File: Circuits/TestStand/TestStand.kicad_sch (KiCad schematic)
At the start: 2 parts, among them U1 INA125UA

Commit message: HX711 Load Cell Circuitry
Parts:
- removed U1: INA125UA, D16, symbol 2024-08-07_02-08-08:INA125UA
- added C1, C2, C4: 0.1uF, symbol Device:C
- added C3: 10uF, symbol Device:C
- added J1: Screw_Terminal_01x07, symbol Connector:Screw_Terminal_01x07
- added JP1: SolderJumper_2_Bridged, symbol Jumper:SolderJumper_2_Bridged
- added L1: 3.3uH, symbol Device:L
- added Q1: MMBT4403-7-F, SOT96P240X110-3N, symbol MMBT4403-7-F:MMBT4403-7-F
- added R2, R3: 100, symbol Device:R_US
- added R4, R5: 8.2K, symbol Device:R_US
- added U1: HX711, Package_SO:SOP-16_3.9x9.9mm_P1.27mm, symbol Analog_ADC:HX711
- R1: value 10 -> 10K
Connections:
- net at R1.1: now also JP1.2 (B), U1.15 (RATE)
- net +5V: now reaches R1.2
- net +5V: now also Q1.2, U1.1 (VSUP), U1.16 (DVDD)
- new net: C1.1, R3.2, U1.7 (INA-)
- new net: C1.2, R2.2, U1.8 (INA+)
- new net: L1.2, U1.3 (AVDD)
- new net: Q1.1, U1.2 (BASE)
- new net: Q1.3, R5.1
- new net: R4.2, R5.2, U1.4 (VFB)
- new net: C2.1, U1.6 (VBG)
- new net A+: J1.4 (Pin_4), R2.1
- new net A-: J1.5 (Pin_5), R3.1
- new net B+: J1.1 (Pin_1), U1.10 (INB+)
- new net B-: J1.2 (Pin_2), U1.9 (INB-)
- new net DAT: U1.12 (DOUT)
- new net E+: C3.1, C4.1, J1.7 (Pin_7), L1.1
- new net GND: C2.2, C3.2, C4.2, J1.3 (Pin_3), J1.6 (Pin_6), JP1.1 (A), R4.1, U1.14 (XI), U1.5 (AGND)
- new net SCK: U1.11 (PD_SCK)
- no-connect marks 0 -> 1
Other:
- note added: "Closed: 10SPS Open: 80SPS"
- note added: "Load Cell 0 IO and Amplifier"

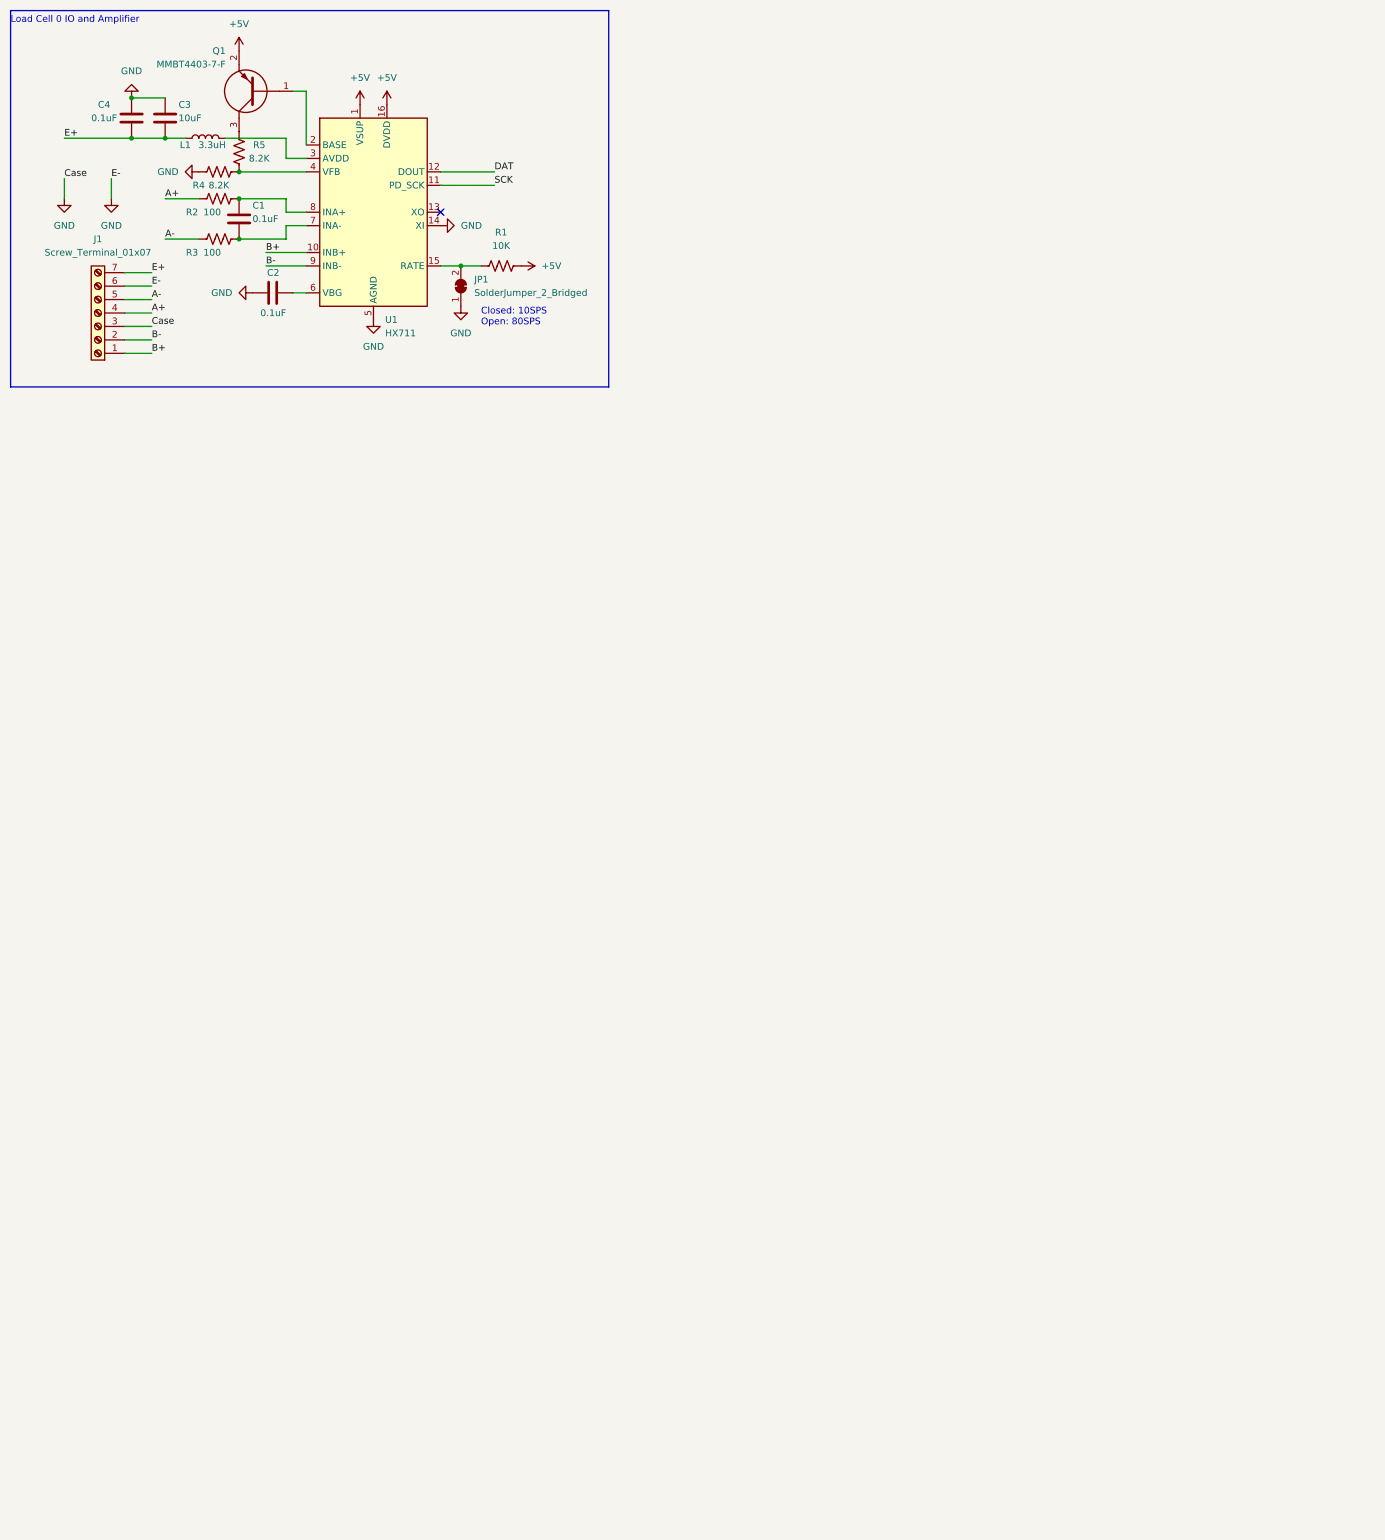
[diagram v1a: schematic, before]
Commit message: Added all 3 load cell amplifiers
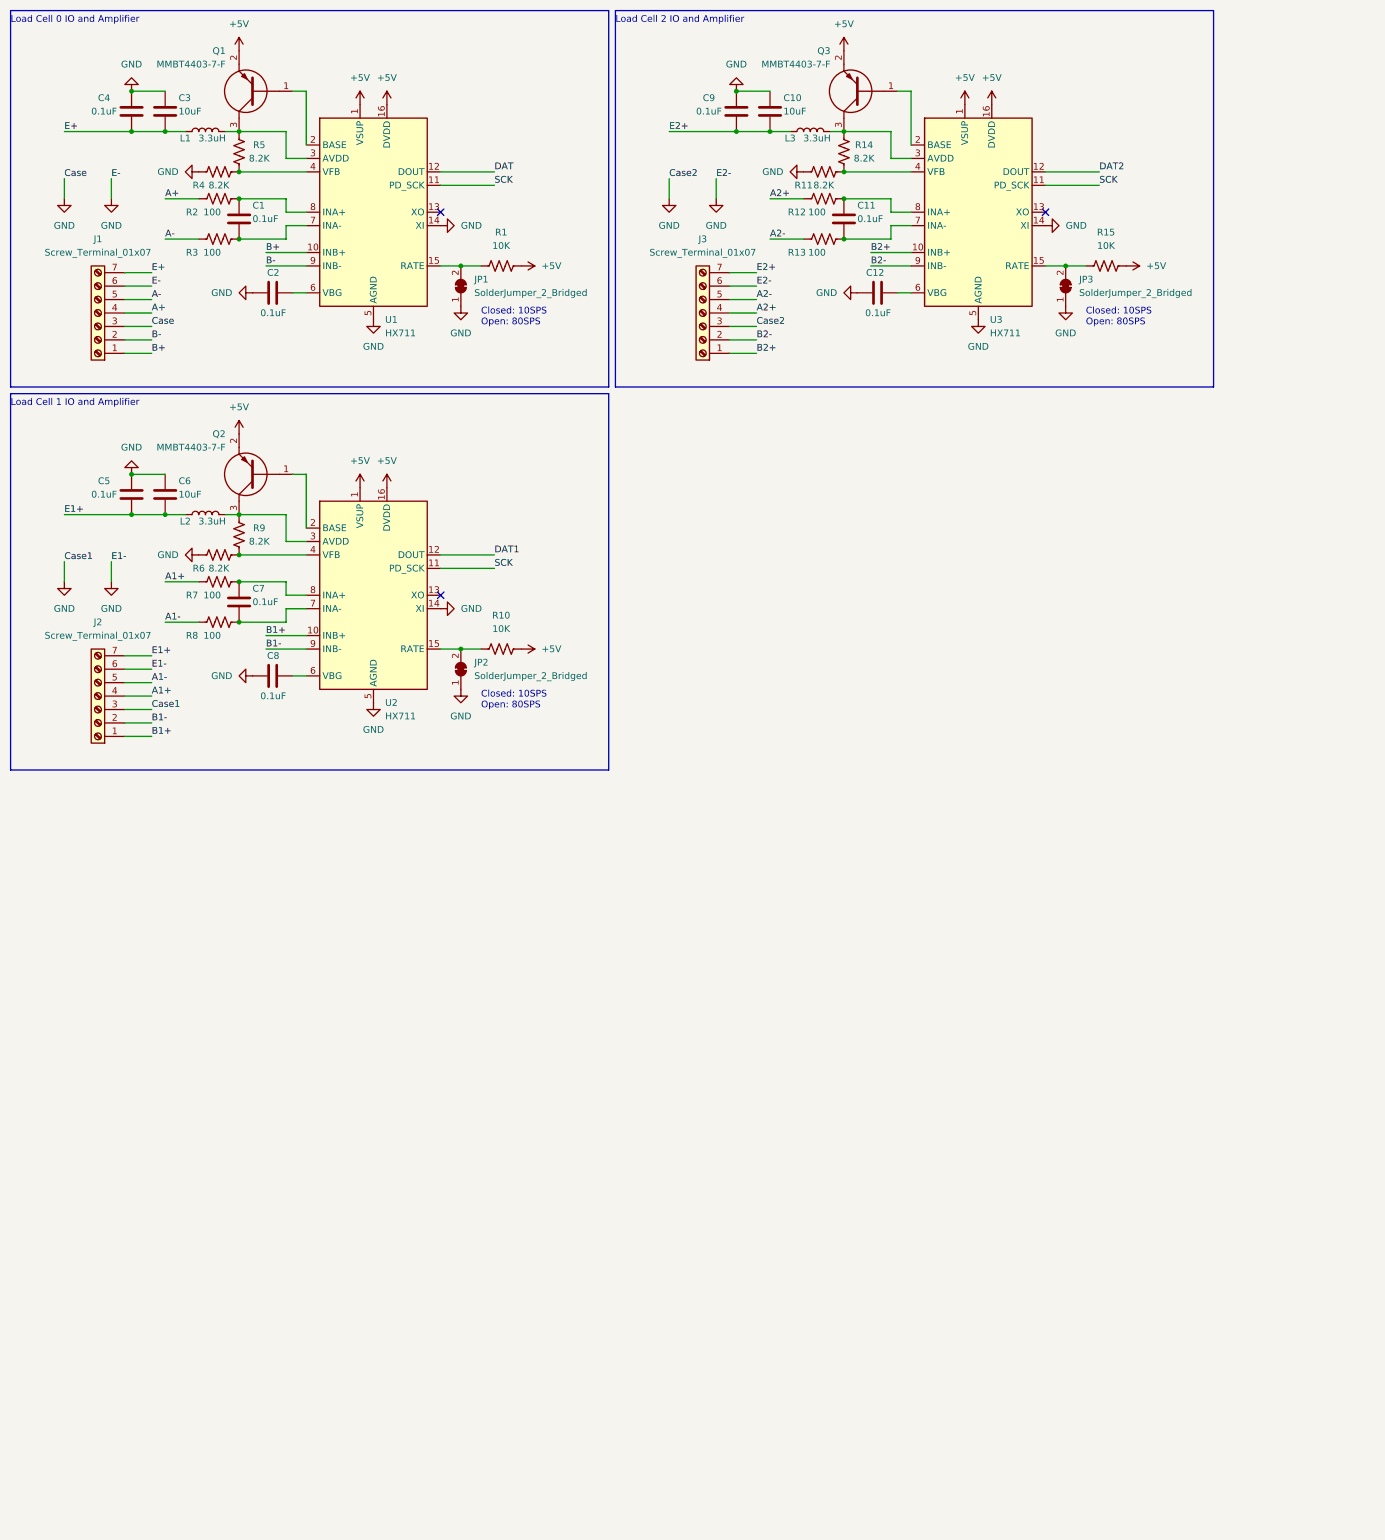
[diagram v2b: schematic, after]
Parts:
- added C10, C6: 10uF, symbol Device:C
- added C11, C12, C5, C7, C8, C9: 0.1uF, symbol Device:C
- added J2, J3: Screw_Terminal_01x07, symbol Connector:Screw_Terminal_01x07
- added JP2, JP3: SolderJumper_2_Bridged, symbol Jumper:SolderJumper_2_Bridged
- added L2, L3: 3.3uH, symbol Device:L
- added Q2, Q3: MMBT4403-7-F, SOT96P240X110-3N, symbol MMBT4403-7-F:MMBT4403-7-F
- added R10, R15: 10K, symbol Device:R_US
- added R11, R14, R6, R9: 8.2K, symbol Device:R_US
- added R12, R13, R7, R8: 100, symbol Device:R_US
- added U2, U3: HX711, Package_SO:SOP-16_3.9x9.9mm_P1.27mm, symbol Analog_ADC:HX711
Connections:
- net +5V: now also Q2.2, Q3.2, R10.2, R15.2, U2.1 (VSUP), U2.16 (DVDD), U3.1 (VSUP), U3.16 (DVDD)
- net GND: now also C10.2, C12.2, C5.2, C6.2, C8.2, C9.2, J2.3 (Pin_3), J2.6 (Pin_6), J3.3 (Pin_3), J3.6 (Pin_6), JP2.1 (A), JP3.1 (A), R11.1, R6.1, U2.14 (XI), U2.5 (AGND), U3.14 (XI), U3.5 (AGND)
- net SCK: now also U2.11 (PD_SCK), U3.11 (PD_SCK)
- net at L1.2, U1.3 (AVDD): now also Q1.3, R5.1
- new net: C11.1, R13.2, U3.7 (INA-)
- new net: C11.2, R12.2, U3.8 (INA+)
- new net: C7.1, R8.2, U2.7 (INA-)
- new net: C7.2, R7.2, U2.8 (INA+)
- new net: Q3.1, U3.2 (BASE)
- new net: L3.2, Q3.3, R14.1, U3.3 (AVDD)
- new net: R6.2, R9.2, U2.4 (VFB)
- new net: L2.2, Q2.3, R9.1, U2.3 (AVDD)
- new net: JP2.2 (B), R10.1, U2.15 (RATE)
- new net: Q2.1, U2.2 (BASE)
- new net: C8.1, U2.6 (VBG)
- new net: JP3.2 (B), R15.1, U3.15 (RATE)
- new net: R11.2, R14.2, U3.4 (VFB)
- new net: C12.1, U3.6 (VBG)
- new net A1+: J2.4 (Pin_4), R7.1
- new net A1-: J2.5 (Pin_5), R8.1
- new net A2+: J3.4 (Pin_4), R12.1
- new net A2-: J3.5 (Pin_5), R13.1
- new net B1+: J2.1 (Pin_1), U2.10 (INB+)
- new net B1-: J2.2 (Pin_2), U2.9 (INB-)
- new net B2+: J3.1 (Pin_1), U3.10 (INB+)
- new net B2-: J3.2 (Pin_2), U3.9 (INB-)
- new net DAT1: U2.12 (DOUT)
- new net DAT2: U3.12 (DOUT)
- new net E1+: C5.1, C6.1, J2.7 (Pin_7), L2.1
- new net E2+: C10.1, C9.1, J3.7 (Pin_7), L3.1
- no-connect marks 1 -> 3
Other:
- note added: "Load Cell 1 IO and Amplifier"
- note added: "Load Cell 2 IO and Amplifier"
- moved on the sheet: C3, C4, L1

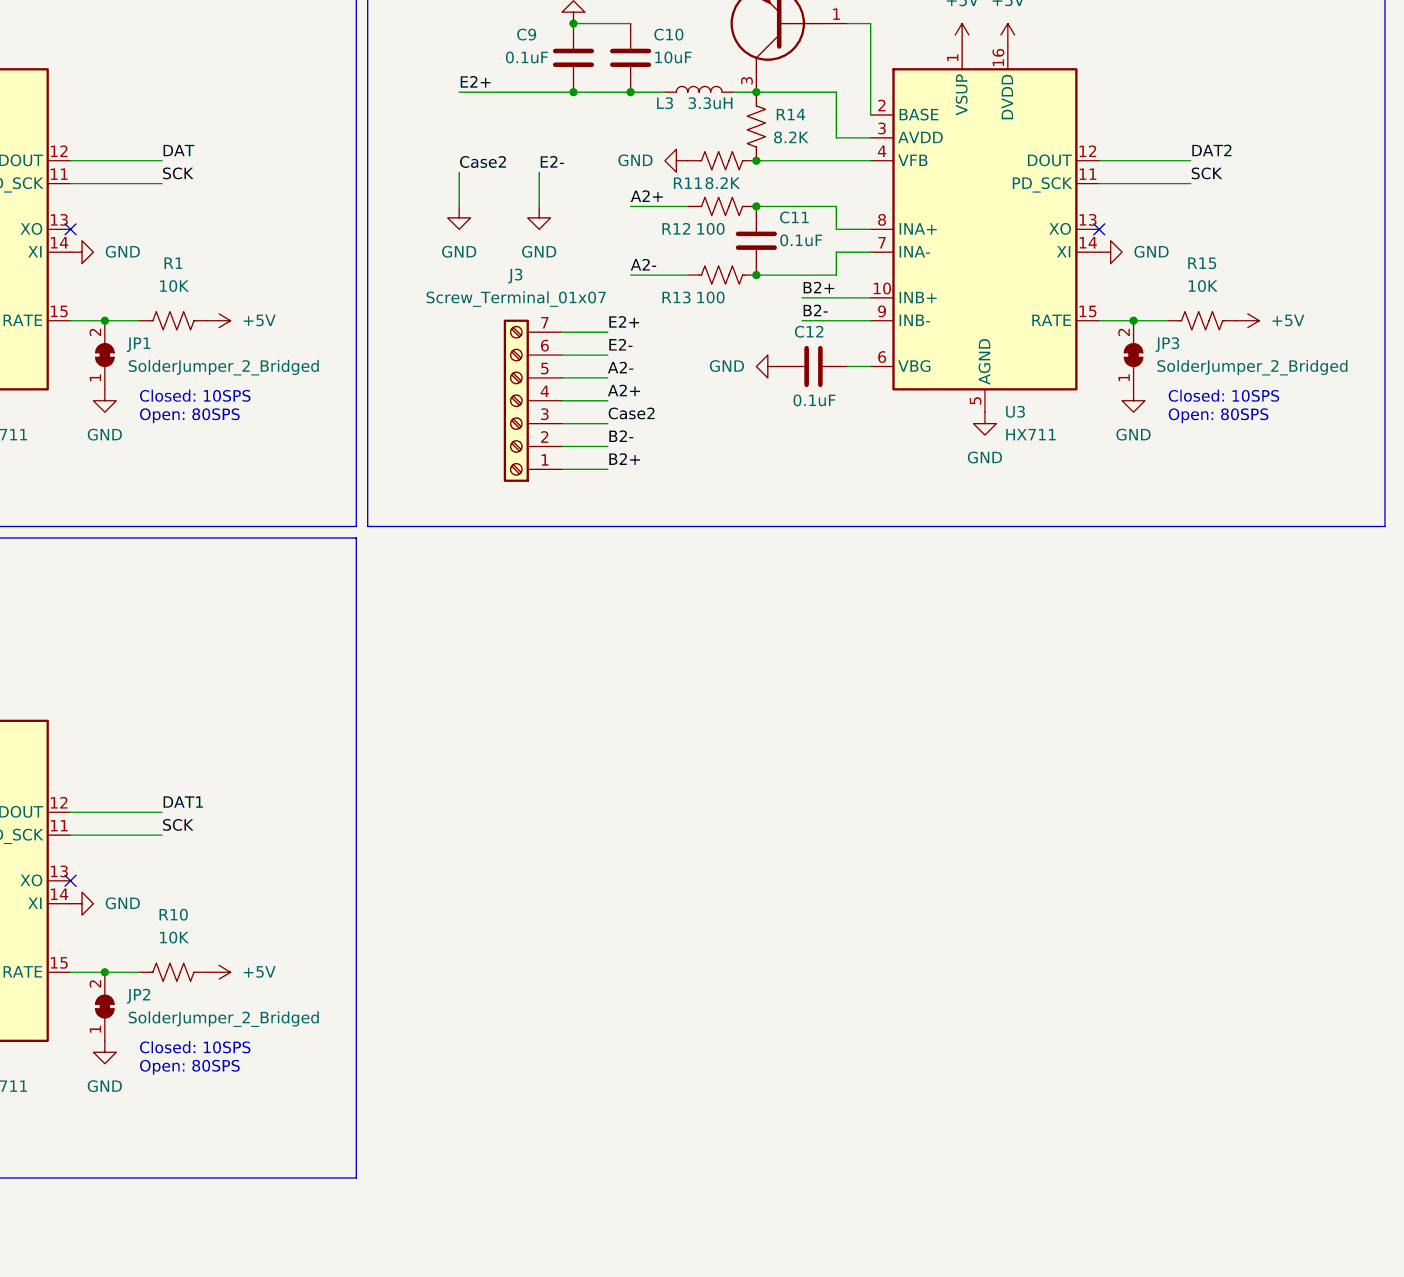
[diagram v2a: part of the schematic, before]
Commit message: Added rpi to schematic
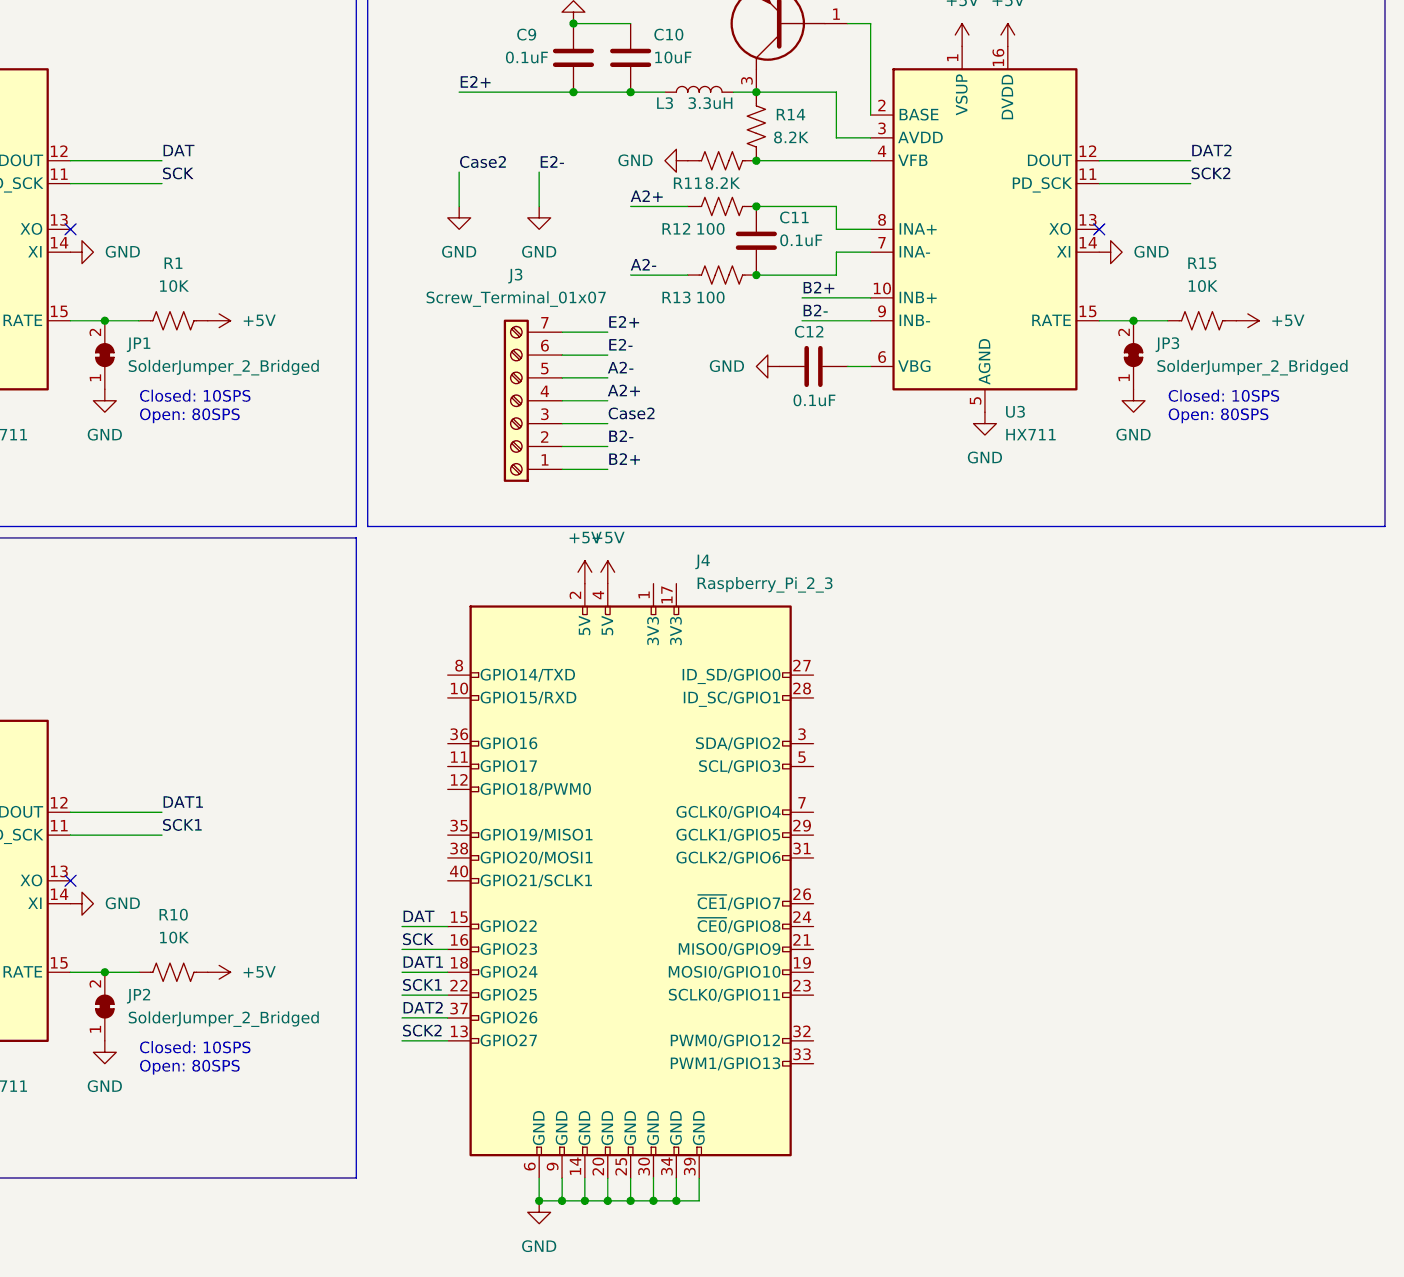
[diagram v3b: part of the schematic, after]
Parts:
- added J4: Raspberry_Pi_2_3, symbol Connector:Raspberry_Pi_2_3
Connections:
- net +5V: now also J4.2 (5V), J4.4 (5V)
- net DAT: now also J4.15 (GPIO22)
- net DAT1: now also J4.18 (GPIO24)
- net DAT2: now also J4.37 (GPIO26)
- net GND: now also J4.14 (GND), J4.20 (GND), J4.25 (GND), J4.30 (GND), J4.34 (GND), J4.39 (GND), J4.6 (GND), J4.9 (GND)
- net SCK: now also J4.16 (GPIO23); no longer U2.11 (PD_SCK), U3.11 (PD_SCK)
- new net SCK1: J4.22 (GPIO25), U2.11 (PD_SCK)
- new net SCK2: J4.13 (GPIO27), U3.11 (PD_SCK)
